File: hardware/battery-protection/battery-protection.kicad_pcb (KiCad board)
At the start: 2 copper layers, 90 x 60 mm, 28 parts, among them J1 M6 Battery input, J2 M5 Ground, J3 M5 Output, J4 M5 Output, J5 M5 Output, Q1 Q_PMOS_GDS, Q1 Q_PMOS_SGD, Q2 Q_PMOS_GDS, Q2 Q_PMOS_SGD, Q3 Q_PMOS_GDS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

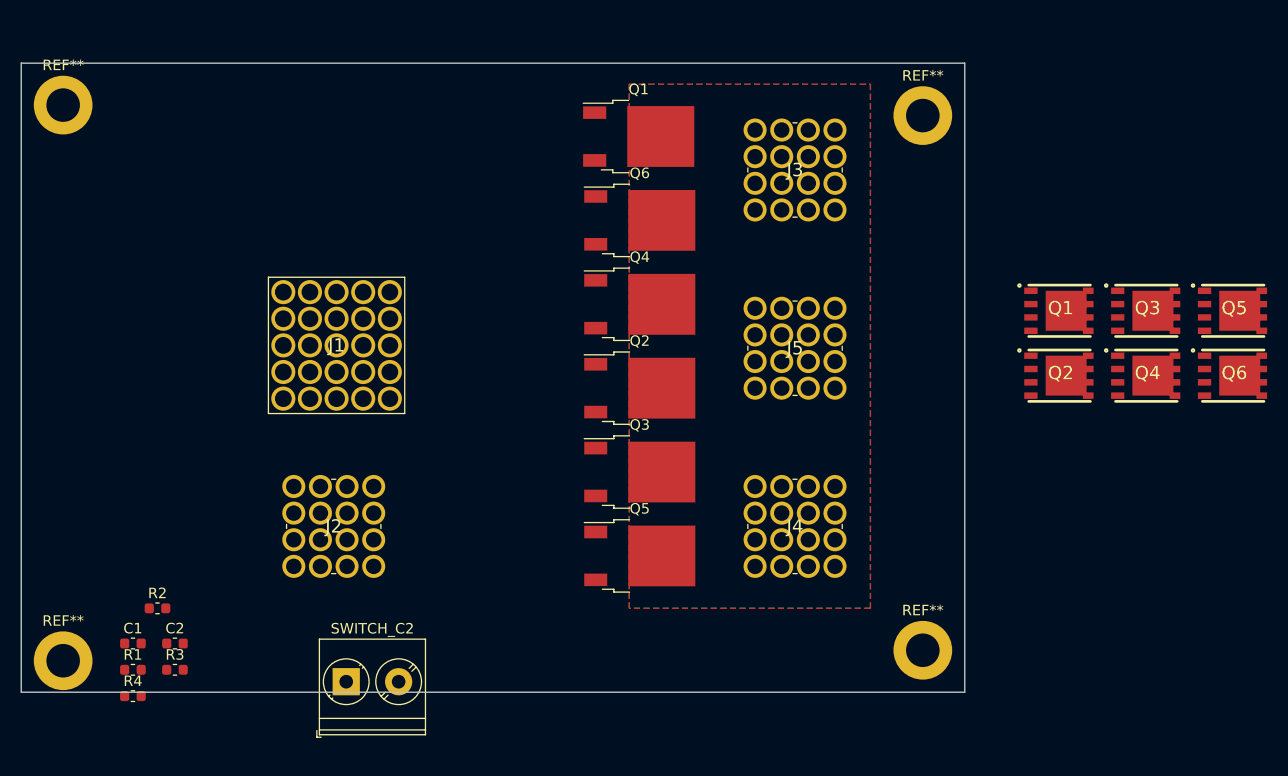
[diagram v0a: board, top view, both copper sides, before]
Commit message: Finished routing battery protection
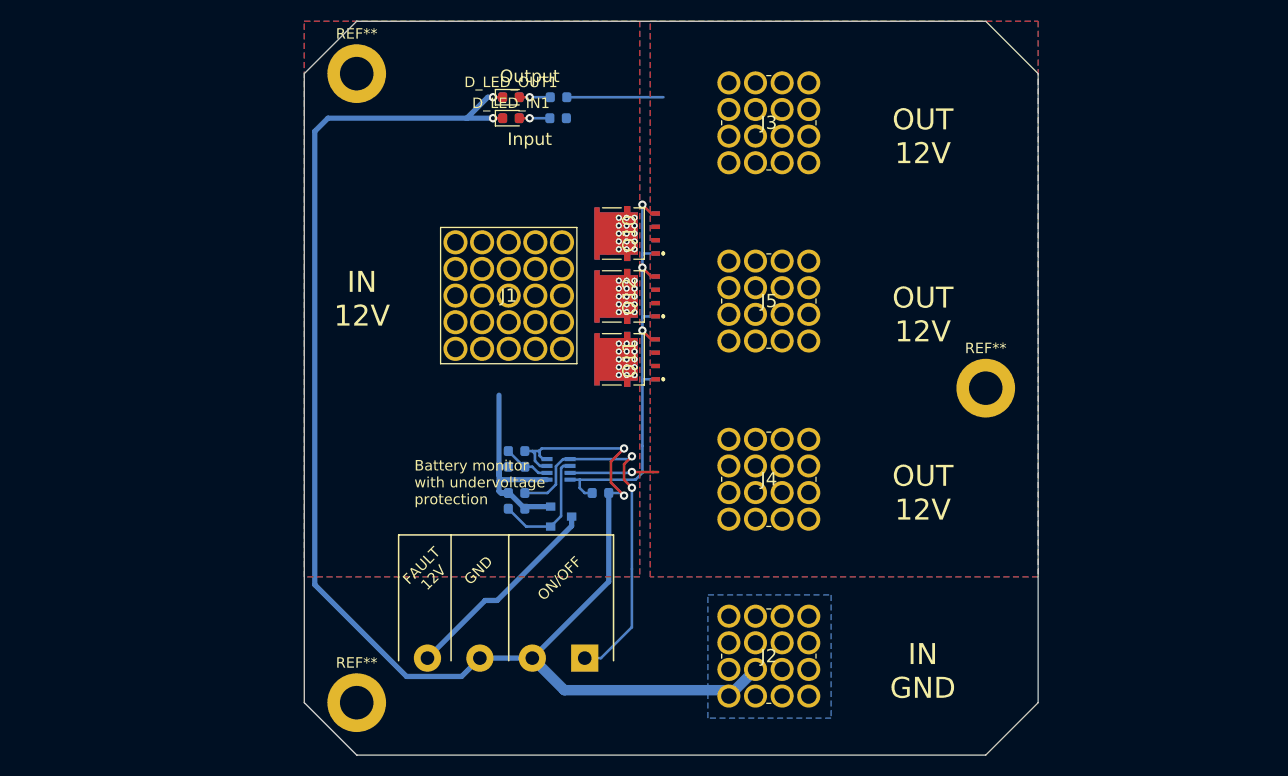
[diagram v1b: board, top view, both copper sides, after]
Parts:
- removed C1, C2: C_Small, Capacitor_SMD:C_0603_1608Metric
- removed Q1, Q2, Q3, Q4, Q5, Q6: Q_PMOS_GDS, Package_TO_SOT_SMD:TO-252-2
- removed Q1, Q2, Q3, Q4, Q5, Q6: Q_PMOS_SGD, mosfet:POWERPAKSO-8
- removed R3: R_Small, Resistor_SMD:R_0603_1608Metric
- removed R4: 10k, Resistor_SMD:R_0603_1608Metric
- removed the REF** at (74.0, 94.0)
- removed the REF** at (74.0, 147.0)
- removed the REF** at (156.0, 146.0)
- removed the REF** at (156.0, 95.0)
- removed SWITCH_C2: Remote, TerminalBlock_Phoenix:TerminalBlock_Phoenix_PT-1,5-2-5.0-H_1x02_P5.00mm_Horizontal
- added D_LED_IN1: 2V, LED_SMD:LED_0603_1608Metric, F.Cu at (116.7, 95.2)
- added D_LED_OUT1: 2V, LED_SMD:LED_0603_1608Metric, F.Cu at (116.7, 93.2)
- added FAULT_PU1: 10k, Resistor_SMD:R_0603_1608Metric, B.Cu at (117.2, 132.5)
- added G_PD1: 10k, Resistor_SMD:R_0603_1608Metric, B.Cu at (125.2, 131.0)
- added J6: Control, TerminalBlock_Phoenix:TerminalBlock_Phoenix_MKDS-1,5-4_1x04_P5.00mm_Horizontal, B.Cu at (123.8, 146.8)
- added Q10: Q_NMOS_SGD, mosfet:SQJA72EPT1_GE3, F.Cu at (129.4, 106.2)
- added Q11: Q_NMOS_SGD, mosfet:SQJA72EPT1_GE3, F.Cu at (129.4, 118.2)
- added Q12: Q_NMOS_SGD, mosfet:SQJA72EPT1_GE3, F.Cu at (129.4, 112.2)
- added Q13: IRLML6402, Package_TO_SOT_SMD:SOT-23, B.Cu at (121.5, 133.2)
- added Q7: Q_NMOS_SGD, mosfet:SQJA72EPT1_GE3, B.Cu at (129.4, 112.2)
- added Q8: Q_NMOS_SGD, mosfet:SQJA72EPT1_GE3, B.Cu at (129.4, 118.2)
- added Q9: Q_NMOS_SGD, mosfet:SQJA72EPT1_GE3, B.Cu at (129.4, 106.2)
- added REF**: MountingHole_3.2mm_M3_DIN965_Pad, MountingHole:MountingHole_3.2mm_M3_DIN965_Pad, F.Cu at (162.0, 121.0)
- added REF**: MountingHole_3.2mm_M3_DIN965_Pad, MountingHole:MountingHole_3.2mm_M3_DIN965_Pad, F.Cu at (102.0, 91.0)
- added REF**: MountingHole_3.2mm_M3_DIN965_Pad, MountingHole:MountingHole_3.2mm_M3_DIN965_Pad, F.Cu at (102.0, 151.0)
- added R_LED_IN1: 680R, Resistor_SMD:R_0603_1608Metric, B.Cu at (121.2, 95.2)
- added R_LED_OUT1: 680R, Resistor_SMD:R_0603_1608Metric, B.Cu at (121.2, 93.2)
- added SHDN_PU1: 10k, Resistor_SMD:R_0603_1608Metric, B.Cu at (117.2, 131.0)
- added U1: LTC4365TS8, Package_TO_SOT_SMD:SOT-23-8, B.Cu at (121.2, 128.8)
- UV1: renamed from R1; value R_Small -> 10k; moved to B.Cu
- UV2: renamed from R2; value R_Small -> 470R; moved to B.Cu
- moved J2 43.3 mm to (137.5, 150.4)
- moved UV1 41.4 mm to (117.2, 128.5)
- moved UV2 37.4 mm to (117.2, 127.0)
- moved J1 17.1 mm to (111.4, 117.2)
- moved J3 5.15 mm to (137.5, 99.5)
- moved J4 5.15 mm to (137.5, 133.5)
- moved J5 5.15 mm to (137.5, 116.5)
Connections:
- UV2 pad 2: Net-(C2-Pad1) -> GND
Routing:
- net GND: track 0.00 -> 153.7 mm, vias 0 -> 4
- net gate_driver: track 0.00 -> 43.7 mm, vias 0 -> 3
- net ~SHDN: track 0.00 -> 36.3 mm, vias 0 -> 2
- net 12V_in: track 0.00 -> 23.9 mm, vias 0 -> 45
- net ~FAULT: track 0.00 -> 19.9 mm
- net 12V_out: track 0.00 -> 17.6 mm, vias 0 -> 1
- net Net-(FAULT_PU1-Pad1): track 0.00 -> 11.7 mm
- net Net-(U1-Pad2): track 0.00 -> 4.55 mm
- net Net-(D_LED_IN1-Pad2): track 0.00 -> 2.92 mm, vias 0 -> 1
- net Net-(D_LED_OUT1-Pad2): track 0.00 -> 2.71 mm, vias 0 -> 1
- added copper zone on B.Cu, net 12V_in
- added copper zone on F.Cu, net 12V_in
- added copper zone on B.Cu, net GND
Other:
- board size 90 x 60 mm -> 70 x 70 mm
- board text added: "Battery monitor with undervoltage protection"
- board text added: "Electrical specification Input 5 - 30 V Mosfet Rds@8V - 0.2 mOhm Junction to ambient 1 deg/A"
- board text added: "FAULT 12V"
- board text added: "GND"
- board text added: "IN 12V"
- board text added: "IN GND"
- board text added: "Input"
- board text added: "ON/OFF"
- board text added: "OUT 12V"
- board text added: "Output"

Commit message: Added aluminum block to batteryprotection
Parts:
- moved J6 25.2 mm to (148.8, 149.5)
- moved J2 24.8 mm to (112.8, 149.5)
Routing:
- net ~SHDN: track 36.3 -> 50.7 mm
- net GND: track 153.7 -> 155.4 mm
- net ~FAULT: track 19.9 -> 20.9 mm

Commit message: Changed to pd for mcu and added pinout for led
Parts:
- removed FAULT_PU1, SHDN_PU1: 10k, Resistor_SMD:R_0603_1608Metric
- removed Q13: IRLML6402, Package_TO_SOT_SMD:SOT-23
- added SHDN_PD1: 10k, Resistor_SMD:R_0603_1608Metric, B.Cu at (117.2, 130.8)
- added UV3: 100pF, Capacitor_SMD:C_0603_1608Metric, B.Cu at (117.2, 125.2)
- J6: value Control -> CTRL; footprint TerminalBlock_Phoenix:TerminalBlock_Phoenix_MKDS-1,5-4_1x04_P5.00mm_Horizontal -> TerminalBlock_Phoenix:TerminalBlock_Phoenix_MKDS-1,5-6_1x06_P5.00mm_Horizontal
- moved J6 11.7 mm to (138.0, 145.0), turned to 0 degrees
- moved UV1 0.25 mm to (117.2, 128.2)
- moved UV2 0.25 mm to (117.2, 126.8)
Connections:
- J6 pad 1: ~SHDN -> 12V_in
- J6 pad 2: GND -> ~SHDN
- J6 pad 3: GND -> 12V_in
- J6 pad 4: ~FAULT -> GND
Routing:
- net GND: track 155.4 -> 124.5 mm
- net 12V_in: track 23.9 -> 49.3 mm
- net ~FAULT: track 20.9 -> 0.00 mm
- net Net-(U1-Pad6): track 11.7 -> 0.00 mm
- net ~SHDN: track 50.7 -> 41.2 mm
- net 12V_out: track 17.6 -> 24.6 mm
- net Net-(U1-Pad2): track 4.55 -> 6.15 mm
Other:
- board text added: "+ -"
- board text added: "Electrical specification Input 5 - 30 V Current <100 A Approx resistanse 0.35 mOhm"
- board text added: "LED INPUT"
- board text added: "LED OUTPUT"
- board text added: "Rev 1.1 2020-07-30"
- board text removed: "Electrical specification Input 5 - 30 V Mosfet Rds@8V - 0.2 mOhm Junction to ambient 1 deg/A"
- board text removed: "FAULT 12V"
- board text removed: "GND"
